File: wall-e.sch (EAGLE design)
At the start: 38 parts, among them IC1 VREG-TS1117CW-3V3, U1 TSM2306CX, U2 TSM2306CX, U3 TSM2306CX, U4 TSM2306CX, U5 TSM2306CX, U6 TSM2306CX, U7 TSM2306CX

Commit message: Addition of the AX12 control circuit and battery manager
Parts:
- removed C13: 4.7uF, rcl:C-EUC0805
- removed DRV8835_7-10, DRV8835_POWER: (no value), pinhead:PINHD-1X4
- removed JP2: (no value), pinhead:PINHD-1X2
- added AX12, AX12-2: 5267-3, con-molex-spox:5267-3
- added BATT: (no value), con-phoenix-500:MSTBV2
- added D8, D9: (no value), diode:DIODE-SOD523
- added LD1: (no value), led:DUOLED-RG-A
- added ON/OFF: SWITCH, switch:SWITCH
- added R10: 47K, resistor:R-US_R0805
- added R11: 51K, resistor:R-US_R0805
- added R12: 13K, resistor:R-US_R0805
- added R13: 130K, resistor:R-US_R0805
- added R14, R15: 1K, resistor:R-US_R0805
- added R16: 2.2K, resistor:R-US_R0805
- added R17: 220R, resistor:R-US_R0805
- added R18: 10K, resistor:R-US_R0805
- added R8: 348R, resistor:R-US_R0805
- added R9: 22K, resistor:R-US_R0805
- added T1: BC847, transistor:BC847
- added U$2: REGUL_PTH, regul_pth:REGUL_PTH
- added U8: LM293AD, LM293ADR:LM293AD
- added U9: TSM2306CX, tsm2306:TSM2306CX
- C10, C9: value 100nF -> 220uF; device rcl:C-EUC0805 -> resistor:CPOL-USE2.5-7
- C11: value 100nF -> 100n; device rcl:C-EUC0805 -> resistor:C-USC0805
- C12: value 10uF -> 100n; device rcl:C-EUC0805 -> resistor:C-USC0805
- R6, R7: value 100k -> 470
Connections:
- removed net SWCLK: JP2.2, U$1.PA14
- removed net SWD: JP2.1, U$1.PA13
- new net AX12_RX: D8.A, R17.1
- new net AX12_TX: R18.2, T1.C
- new net N$12: C10.+, LD1.A, R11.2, U$2.VO
- new net N$13: R8.2, U$2.VADJ
- new net N$14: R15.2, U8.1OUT
- new net N$15: LD1.CR, R15.1
- new net N$16: R14.2, U8.2OUT
- new net N$17: LD1.CG, R14.1
- new net N$19: C11.1, R10.1, R9.2, U8.1IN+, U8.2IN-
- new net N$20: R11.1, R12.2, U8.1IN-
- new net N$21: C12.1, R12.1, R13.2, U8.2IN+
- new net N$22: D9.C, R16.1, R17.2
- new net N$23: AX12-2.-3, AX12.-3, U9.D
- new net N$24: R16.2, T1.B
- new net N$25: D9.A, T1.E, U9.S
- new net N$29: D8.C, R18.1
- new net N$30: BATT-1.SK, ON/OFF.3
- new net VCC: U8.VCC
- net +12V: now also AX12-2.-2, AX12.-2, C9.+, ON/OFF.1, ON/OFF.2, R10.2, U$2.VI
- net +3V3: now also U9.G; no longer C10.1, C11.1, C12.1, C13.1, C9.1
- net +5V: no longer DRV8835_POWER.1, DRV8835_POWER.4
- net GND: now also AX12-2.-1, AX12.-1, BATT-2.SK, C10.-, C9.-, R13.1, R8.1, R9.1, U$2.GND, U8.GND; no longer C10.2, C13.2, C9.2, DRV8835_POWER.2, DRV8835_POWER.3
- net LED1: now also U$1.PF0/OSC_IN; no longer U$1.PB10
- net LED2: now also U$1.PF1/OSC_OUT; no longer U$1.PB11
- net MOTOR1_PWM: no longer DRV8835_7-10.2
- net MOTOR1_PWM_N: no longer DRV8835_7-10.4
- net MOTOR2_PWM: no longer DRV8835_7-10.1
- net MOTOR2_PWM_N: no longer DRV8835_7-10.3
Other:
- moved on the sheet: C11, C12

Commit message: Cleaning of the schematic
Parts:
- removed JP1: (no value), pinhead:PINHD-2X5
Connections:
- removed net N$12: C10.+, LD1.A, R11.2, U$2.VO
- removed net N$18: TOIT-3.1
- new net SWCLK: U$1.PA14
- new net SWDIO: U$1.PA13
- net +5V: now also C10.+, LD1.A, R11.2, U$2.VO; no longer JP1.2, JP1.4
- net AX12-RX: no longer JP1.8
- net AX12-TX: no longer JP1.10
- net GND: now also TOIT-3.1; no longer JP1.6, JP1.9
- net LED1: now also U$1.PB10; no longer U$1.PF0/OSC_IN
- net LED2: now also U$1.PB11; no longer U$1.PF1/OSC_OUT
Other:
- note added: "+12V/+5V/+3.3V"
- note added: "AX12 CONNECTOR"
- note added: "BATTERY LEVEL"
- note added: "CODEUSES CONNECTOR"
- note added: "DISTANCE SENSORS CONNECTOR"
- note added: "IMU CONNECTOR"
- note added: "MOTOR CONTROL"
- note added: "POWER SUPPLY"
- note added: "ROOF CONNECTOR"
- moved on the sheet: AX12, AX12-2, BATT-1, BATT-2, C1, C10, C11, C12, C2, C9, CODEUSE-1, CODEUSE-2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

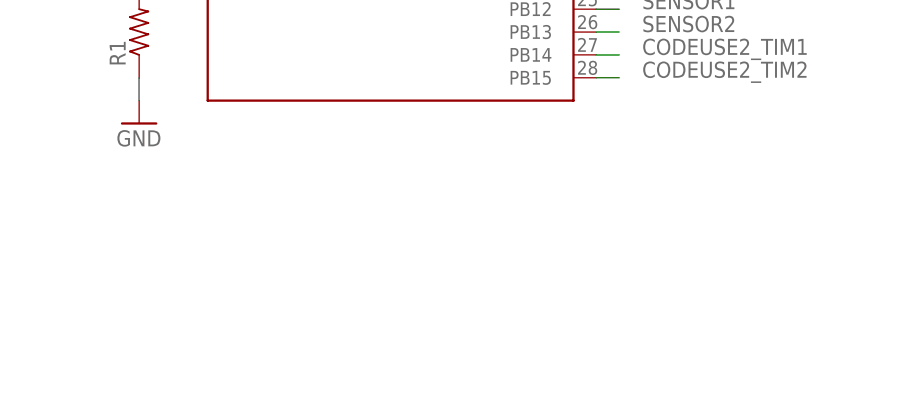
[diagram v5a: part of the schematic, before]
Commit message: Update of the SWD connector
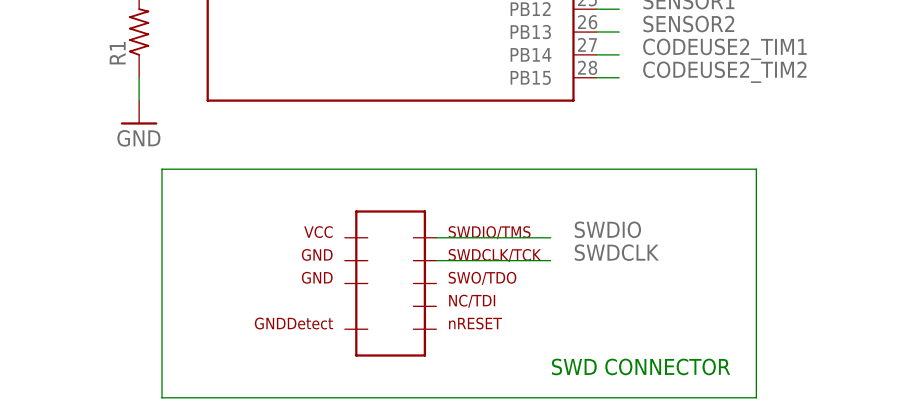
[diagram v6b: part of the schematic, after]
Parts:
- added U$3: SWD/JTAG-_PINS, TelecomRobotics:SWD/JTAG-_PINS
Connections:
- new net SWDCLK: U$3.P$4
- net SWDIO: now also U$3.P$2
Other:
- note added: "SWD CONNECTOR"
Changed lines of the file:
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@@
 <part name="GND10" library="supply1" deviceset="GND" device=""/>
 <part name="P+10" library="supply1" deviceset="+5V" device=""/>
+<part name="U$3" library="TelecomRobotics" deviceset="SWD/JTAG-_PINS" device=""/>
 </parts>
 <sheets>
@@
 <wire x1="175.26" y1="7.62" x2="121.92" y2="7.62" width="0.1524" layer="254"/>
 <text x="154.94" y="-22.86" size="1.778" layer="254">IMU CONNECTOR</text>
+<text x="78.74" y="-25.4" size="1.778" layer="91">SWD CONNECTOR</text>
 </plain>
 <instances>
@@
 <instance part="GND10" gate="1" x="134.62" y="45.72"/>
 <instance part="P+10" gate="1" x="-45.72" y="45.72"/>
+<instance part="U$3" gate="G$1" x="60.96" y="-15.24"/>
 </instances>
 <busses>
@@
 <label x="88.9" y="58.42" size="1.778" layer="95"/>
 </segment>
+<segment>
+<pinref part="U$3" gate="G$1" pin="P$2"/>
+<wire x1="66.04" y1="-10.16" x2="78.74" y2="-10.16" width="0.1524" layer="91"/>
+<label x="81.28" y="-10.16" size="1.778" layer="95"/>
+</segment>
 </net>
 <net name="SWCLK" class="0">
@@
 </segment>
 </net>
+<net name="SWDCLK" class="0">
+<segment>
+<pinref part="U$3" gate="G$1" pin="P$4"/>
+<wire x1="66.04" y1="-12.7" x2="78.74" y2="-12.7" width="0.1524" layer="91"/>
+<label x="81.28" y="-12.7" size="1.778" layer="95"/>
+</segment>
+</net>
+<net name="N$10" class="0">
+<segment>
+<wire x1="35.56" y1="-2.54" x2="35.56" y2="-27.94" width="0.1524" layer="91"/>
+<wire x1="35.56" y1="-27.94" x2="101.6" y2="-27.94" width="0.1524" layer="91"/>
+<wire x1="101.6" y1="-27.94" x2="101.6" y2="-2.54" width="0.1524" layer="91"/>
+<wire x1="101.6" y1="-2.54" x2="35.56" y2="-2.54" width="0.1524" layer="91"/>
+</segment>
+</net>

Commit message: Creation of the board
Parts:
- added C13: 4.7uF, rcl:C-EUC0805
- added C4, C5, C6, C7: 100nF, rcl:C-EUC0805
- added C8: 10uF, rcl:C-EUC0805
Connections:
- net +3V3: now also C13.1, C4.1, C5.1, C6.1, C7.1, C8.1
- net GND: now also C13.2, C4.2, C5.2, C6.2, C7.2, C8.2
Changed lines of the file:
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@@
 <part name="P+10" library="supply1" deviceset="+5V" device=""/>
 <part name="U$3" library="TelecomRobotics" deviceset="SWD/JTAG-_PINS" device=""/>
+<part name="C4" library="rcl" deviceset="C-EU" device="C0805" value="100nF"/>
+<part name="C5" library="rcl" deviceset="C-EU" device="C0805" value="100nF"/>
+<part name="C6" library="rcl" deviceset="C-EU" device="C0805" value="100nF"/>
+<part name="C7" library="rcl" deviceset="C-EU" device="C0805" value="100nF"/>
+<part name="C8" library="rcl" deviceset="C-EU" device="C0805" value="10uF"/>
+<part name="C13" library="rcl" deviceset="C-EU" device="C0805" value="4.7uF"/>
+<part name="GND12" library="supply1" deviceset="GND" device=""/>
+<part name="+3V7" library="supply1" deviceset="+3V3" device=""/>
 </parts>
 <sheets>
@@
 <wire x1="175.26" y1="7.62" x2="121.92" y2="7.62" width="0.1524" layer="254"/>
 <text x="154.94" y="-22.86" size="1.778" layer="254">IMU CONNECTOR</text>
-<text x="78.74" y="-25.4" size="1.778" layer="91">SWD CONNECTOR</text>
+<text x="165.1" y="-55.88" size="1.778" layer="91">SWD CONNECTOR</text>
 </plain>
 <instances>
@@
 <instance part="GND10" gate="1" x="134.62" y="45.72"/>
 <instance part="P+10" gate="1" x="-45.72" y="45.72"/>
-<instance part="U$3" gate="G$1" x="60.96" y="-15.24"/>
+<instance part="U$3" gate="G$1" x="147.32" y="-45.72"/>
+<instance part="C4" gate="G$1" x="38.1" y="-25.4"/>
+<instance part="C5" gate="G$1" x="48.26" y="-25.4"/>
+<instance part="C6" gate="G$1" x="58.42" y="-25.4"/>
+<instance part="C7" gate="G$1" x="68.58" y="-25.4"/>
+<instance part="C8" gate="G$1" x="78.74" y="-25.4"/>
+<instance part="C13" gate="G$1" x="88.9" y="-25.4"/>
+<instance part="GND12" gate="1" x="63.5" y="-38.1"/>
+<instance part="+3V7" gate="G$1" x="63.5" y="-15.24"/>
 </instances>
 <busses>
@@
 <pinref part="GND10" gate="1" pin="GND"/>
 </segment>
+<segment>
+<pinref part="C4" gate="G$1" pin="2"/>
+<wire x1="38.1" y1="-30.48" x2="38.1" y2="-33.02" width="0.1524" layer="91"/>
+<wire x1="38.1" y1="-33.02" x2="48.26" y2="-33.02" width="0.1524" layer="91"/>
+<pinref part="C13" gate="G$1" pin="2"/>
+<wire x1="48.26" y1="-33.02" x2="58.42" y2="-33.02" width="0.1524" layer="91"/>
+<wire x1="58.42" y1="-33.02" x2="63.5" y2="-33.02" width="0.1524" layer="91"/>
+<wire x1="63.5" y1="-33.02" x2="68.58" y2="-33.02" width="0.1524" layer="91"/>
+<wire x1="68.58" y1="-33.02" x2="78.74" y2="-33.02" width="0.1524" layer="91"/>
+<wire x1="78.74" y1="-33.02" x2="88.9" y2="-33.02" width="0.1524" layer="91"/>
+<wire x1="88.9" y1="-33.02" x2="88.9" y2="-30.48" width="0.1524" layer="91"/>
+<pinref part="C8" gate="G$1" pin="2"/>
+<wire x1="78.74" y1="-30.48" x2="78.74" y2="-33.02" width="0.1524" layer="91"/>
+<junction x="78.74" y="-33.02"/>
+<pinref part="C7" gate="G$1" pin="2"/>
+<wire x1="68.58" y1="-30.48" x2="68.58" y2="-33.02" width="0.1524" layer="91"/>
+<junction x="68.58" y="-33.02"/>
+<pinref part="C6" gate="G$1" pin="2"/>
+<wire x1="58.42" y1="-30.48" x2="58.42" y2="-33.02" width="0.1524" layer="91"/>
+<junction x="58.42" y="-33.02"/>
+<pinref part="C5" gate="G$1" pin="2"/>
+<wire x1="48.26" y1="-30.48" x2="48.26" y2="-33.02" width="0.1524" layer="91"/>
+<junction x="48.26" y="-33.02"/>
+<wire x1="63.5" y1="-33.02" x2="63.5" y2="-35.56" width="0.1524" layer="91"/>
+<junction x="63.5" y="-33.02"/>
+<pinref part="GND12" gate="1" pin="GND"/>
+</segment>
 </net>
 <net name="+5V" class="0">
@@
 <wire x1="287.02" y1="134.62" x2="287.02" y2="137.16" width="0.1524" layer="91"/>
 <pinref part="+3V11" gate="G$1" pin="+3V3"/>
+</segment>
+<segment>
+<pinref part="C4" gate="G$1" pin="1"/>
+<wire x1="38.1" y1="-22.86" x2="38.1" y2="-20.32" width="0.1524" layer="91"/>
+<wire x1="38.1" y1="-20.32" x2="48.26" y2="-20.32" width="0.1524" layer="91"/>
+<pinref part="C13" gate="G$1" pin="1"/>
+<wire x1="48.26" y1="-20.32" x2="58.42" y2="-20.32" width="0.1524" layer="91"/>
+<wire x1="58.42" y1="-20.32" x2="63.5" y2="-20.32" width="0.1524" layer="91"/>
+<wire x1="63.5" y1="-20.32" x2="68.58" y2="-20.32" width="0.1524" layer="91"/>
+<wire x1="68.58" y1="-20.32" x2="78.74" y2="-20.32" width="0.1524" layer="91"/>
+<wire x1="78.74" y1="-20.32" x2="88.9" y2="-20.32" width="0.1524" layer="91"/>
+<wire x1="88.9" y1="-20.32" x2="88.9" y2="-22.86" width="0.1524" layer="91"/>
+<pinref part="C5" gate="G$1" pin="1"/>
+<wire x1="48.26" y1="-20.32" x2="48.26" y2="-22.86" width="0.1524" layer="91"/>
+<junction x="48.26" y="-20.32"/>
+<pinref part="C6" gate="G$1" pin="1"/>
+<wire x1="58.42" y1="-20.32" x2="58.42" y2="-22.86" width="0.1524" layer="91"/>
+<junction x="58.42" y="-20.32"/>
+<pinref part="C7" gate="G$1" pin="1"/>
+<wire x1="68.58" y1="-20.32" x2="68.58" y2="-22.86" width="0.1524" layer="91"/>
+<junction x="68.58" y="-20.32"/>
+<pinref part="C8" gate="G$1" pin="1"/>
+<wire x1="78.74" y1="-20.32" x2="78.74" y2="-22.86" width="0.1524" layer="91"/>
+<junction x="78.74" y="-20.32"/>
+<wire x1="63.5" y1="-20.32" x2="63.5" y2="-17.78" width="0.1524" layer="91"/>
+<junction x="63.5" y="-20.32"/>
+<pinref part="+3V7" gate="G$1" pin="+3V3"/>
 </segment>
 </net>
@@
 <segment>
 <pinref part="U$3" gate="G$1" pin="P$2"/>
-<wire x1="66.04" y1="-10.16" x2="78.74" y2="-10.16" width="0.1524" layer="91"/>
-<label x="81.28" y="-10.16" size="1.778" layer="95"/>
+<wire x1="152.4" y1="-40.64" x2="165.1" y2="-40.64" width="0.1524" layer="91"/>
+<label x="167.64" y="-40.64" size="1.778" layer="95"/>
 </segment>
 </net>
@@
 <segment>
 <pinref part="U$3" gate="G$1" pin="P$4"/>
-<wire x1="66.04" y1="-12.7" x2="78.74" y2="-12.7" width="0.1524" layer="91"/>
-<label x="81.28" y="-12.7" size="1.778" layer="95"/>
+<wire x1="152.4" y1="-43.18" x2="165.1" y2="-43.18" width="0.1524" layer="91"/>
+<label x="167.64" y="-43.18" size="1.778" layer="95"/>
 </segment>
 </net>
 <net name="N$10" class="0">
 <segment>
-<wire x1="35.56" y1="-2.54" x2="35.56" y2="-27.94" width="0.1524" layer="91"/>
-<wire x1="35.56" y1="-27.94" x2="101.6" y2="-27.94" width="0.1524" layer="91"/>
-<wire x1="101.6" y1="-27.94" x2="101.6" y2="-2.54" width="0.1524" layer="91"/>
-<wire x1="101.6" y1="-2.54" x2="35.56" y2="-2.54" width="0.1524" layer="91"/>
-</segment>
-</net>
+<wire x1="121.92" y1="-33.02" x2="121.92" y2="-58.42" width="0.1524" layer="91"/>
+<wire x1="121.92" y1="-58.42" x2="187.96" y2="-58.42" width="0.1524" layer="91"/>
+<wire x1="187.96" y1="-58.42" x2="187.96" y2="-33.02" width="0.1524" layer="91"/>
+<wire x1="187.96" y1="-33.02" x2="121.92" y2="-33.02" width="0.1524" layer="91"/>
+</segment>
+</net>

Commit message: Corrections following Arnaud's advices.
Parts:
- removed CODEUSE: (no value), con-amp:SMDTOP-4
- removed D8: (no value), diode:DIODE-SOD523
- added C14: 10nF, rcl:C-EUC0805
- added LED1: (no value), led:LEDCHIP-LED0805
- added R19: 10k, rcl:R-US_R0805
- added R20: 2.2K, resistor:R-US_R0805
- added SV2, SV3: (no value), con-lstb:MA05-1
- added SV4, SV5: (no value), con-lstb:MA03-1
- added X2, X3: (no value), con-amp:SMDTOP-4
- C1, C2: value (none) -> 10uF
- C3: value (none) -> 1uF
- R17: value 220R -> 2.2K
- R6, R7: value 470 -> 10k
- R8: value 348R -> 360R
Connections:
- removed net AX12_RX: D8.A, R17.1
- removed net AX12_TX: R18.2, T1.C
- removed net BUTTON4: TOIT-7.1, U$1.PB5
- removed net CODEUSE1_TIM1: CODEUSE-1.1, U$1.PA6
- removed net CODEUSE1_TIM2: CODEUSE-2.1, U$1.PA7
- removed net CODEUSE2_TIM1: CODEUSE-3.1, U$1.PB14
- removed net CODEUSE2_TIM2: CODEUSE-4.1, U$1.PB15
- removed net N$22: D9.C, R16.1, R17.2
- removed net N$29: D8.C, R18.1
- removed net SWDCLK: U$3.P$4
- removed net VCC: U8.VCC
- new net CODEUSE1: U$1.PA7, X2-3.1
- new net CODEUSE1_TIM: U$1.PA6, X2-2.1
- new net CODEUSE2: U$1.PA4, X3-3.1
- new net CODEUSE2_TIM: U$1.PA3, X3-2.1
- new net DEBUG_LED: LED1.A, U$1.PC13
- new net EYE1: SV4.1, U$1.PB14
- new net EYE2: SV5.1, U$1.PB15
- net +3V3: now also C14.2, C3.2, R17.1, R19.2, SV1.1, SV1.2, U$3.P$1, U8.VCC
- net +5V: now also R20.1, SV3.5, SV4.2, SV5.2, X2-1.1, X3-1.1; no longer SV1.1
- net AX12-RX: now also D9.C, R16.1, R18.1
- net AX12-TX: now also R18.2, T1.C
- net GND: now also C14.1, C3.1, LED1.C, SV3.3, SV3.4, SV4.3, SV5.3, U$3.P$3, U$3.P$5, U$3.P$9, X2-4.1, X3-4.1; no longer C3.2
- net MCU_RESET: now also R19.1, TOIT-7.1, U$3.P$10; no longer C3.1
- net MOTOR1_PWM: now also SV2.2
- net MOTOR1_PWM_N: now also SV2.4
- net MOTOR2_PWM: now also SV2.3
- net MOTOR2_PWM_N: now also SV2.5
- net N$23: now also R20.2
- net N$25: now also R17.2
- net PUMP: now also U$1.PB12; no longer U$1.PA8
- net SENSOR1: now also U$1.PB13; no longer U$1.PB12
- net SENSOR2: now also U$1.PA8; no longer U$1.PB13
- net SWCLK: now also U$3.P$4
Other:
- note added: "CODEUSES CONNECTORS"
- note added: "EYES SERVOMOTORS"
- note added: "H BRIDGE"
- note removed: "CODEUSES CONNECTOR"
- moved on the sheet: C3, D1, D2, D3, D7, R17, R18
